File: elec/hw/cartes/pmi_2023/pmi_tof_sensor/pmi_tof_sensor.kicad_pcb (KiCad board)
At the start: 2 copper layers, 30 x 20 mm, 41 parts, among them J1 tof_sensor_female, U1 SN74LVC1T45DBV, U2 TMF8821, U3 VL53L1CXV0FY1, U4 VL53L5CXV0GC

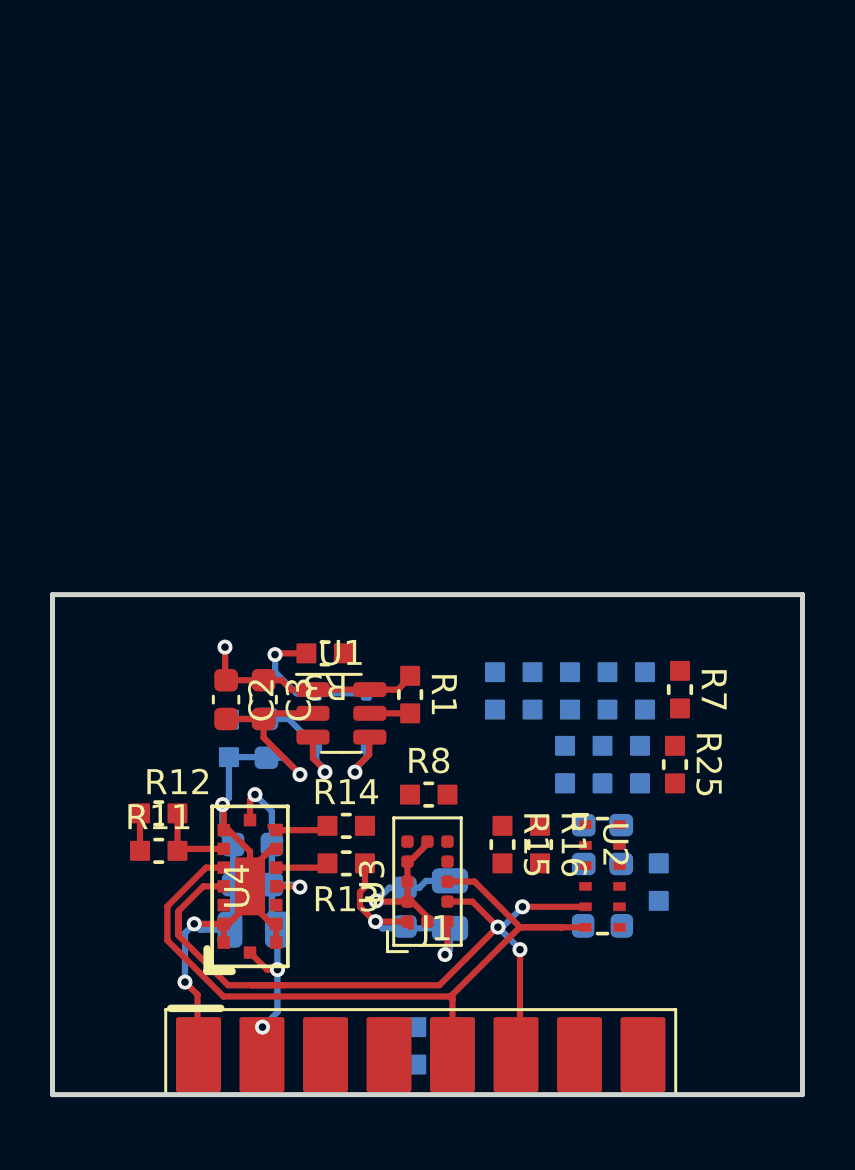
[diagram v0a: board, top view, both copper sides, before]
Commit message: pmi_tof_sensor : last commit before tmf8821 deletion
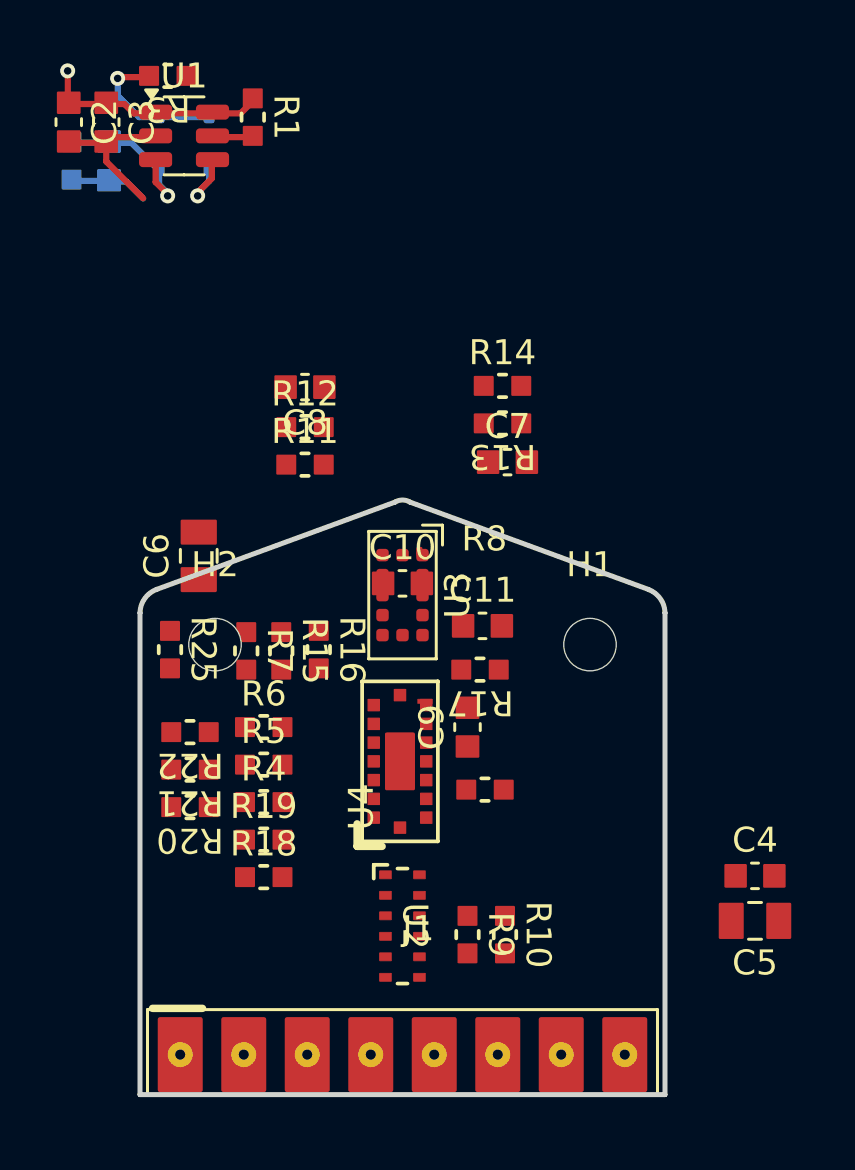
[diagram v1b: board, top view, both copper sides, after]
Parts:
- added H1: MountingHole, cocotter_others:MountingHole_2.1mm, F.Cu at (41.5, 162.0)
- added H2: MountingHole, cocotter_others:MountingHole_2.1mm, F.Cu at (26.5, 162.0)
- C10, C11, C4, C7, C8, C9, R18, R19, R20, R21, R22, R4, R5, R6: moved to F.Cu
- C5, C6: value 10µF 16V -> 10µF 25V; moved to F.Cu
- R1, R13, R14, R15, R16, R2, R25, R3, R7, R8: value 10k -> 10k 1%
- R10, R17, R9: value 10k -> 10k 1%; moved to F.Cu
- moved C1 23.9 mm to (22.3, 142.7)
- moved C2 23.9 mm to (20.6, 141.1)
- moved C3 23.9 mm to (22.1, 141.1)
- moved D1 23.9 mm to (24.3, 141.9)
- moved D2 23.9 mm to (26.3, 141.9)
- moved R1 23.9 mm to (28.0, 140.9)
- moved R2 23.9 mm to (20.8, 142.7)
- moved R3 23.9 mm to (24.6, 139.2)
- moved U1 23.9 mm to (25.3, 141.7)
- moved R25 20.7 mm to (24.7, 162.2)
- moved C7 19.7 mm to (38.2, 154.7), turned to 0 degrees
- moved R13 18.7 mm to (38.0, 153.2)
- moved R14 18.7 mm to (38.0, 151.7)
- moved C8 18.4 mm to (30.1, 151.7)
- moved R22 18.0 mm to (25.5, 165.5), turned to 180 degrees
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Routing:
- net GND: track 44.6 -> 9.56 mm, vias 5 -> 0
- net SCL_3v3: track 31.9 -> 0.00 mm, vias 3 -> 0
- net SDA_3v3: track 30.8 -> 0.00 mm
- net P3V3: track 36.0 -> 9.12 mm, vias 7 -> 1
- net /VL53L5_RSVD6_3v3: track 3.38 -> 0.00 mm
- net /VL53L5_irq_3v3: track 2.12 -> 0.00 mm
- net /VL53L5_I2C_RST_3v3: track 2.12 -> 0.00 mm
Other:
- board size 30 x 20 mm -> 21 x 23.8 mm

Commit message: pmi_tof_sensor : new form factor and enable sequencer
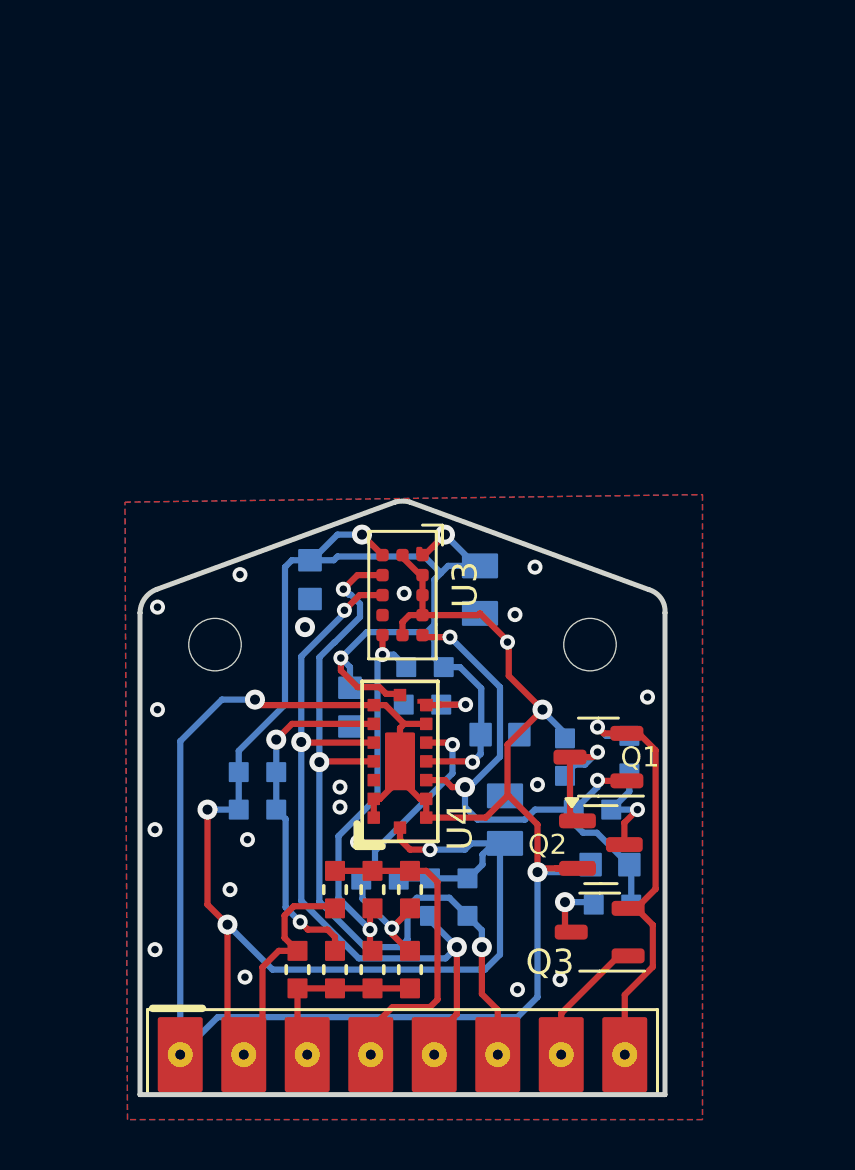
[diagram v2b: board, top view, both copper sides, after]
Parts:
- removed C1, C10, C11, C2, C3: 100nF 50V, cocotter_capacitors:C_0603_1608Metric
- removed D1, D2: 1SS367,H3F, Diode_SMD:D_SOD-323
- removed R1, R2, R3: 10k 1%, cocotter_resistor:r0603_reflow
- removed R19, R22: 0R, cocotter_resistor:r0603_reflow
- removed U1: SN74LVC1T45DBV, Package_TO_SOT_SMD:SOT-23-6
- removed U2: TMF8821, cocotter_ic:TMF882x
- added Q1: BSS84, cocotter_transistors:SOT-23-3, F.Cu at (41.8, 166.5)
- added Q2: 2N7002, Package_TO_SOT_SMD:SOT-23, F.Cu at (41.9, 170.0)
- added Q3: BSS84, cocotter_transistors:SOT-23-3, F.Cu at (41.9, 173.5)
- C4, C5, C6, C7, C8, C9, R10, R11, R12, R13, R14, R8, R9: moved to B.Cu
- R15, R17: value 10k 1% -> 100k; moved to B.Cu
- R16: value 10k 1% -> 3k3 1%; moved to B.Cu
- R18: value 0R -> 100k; moved to B.Cu
- moved C4 21.4 mm to (30.3, 159.4), turned to 90 degrees
- moved R13 18.9 mm to (33.1, 171.4)
- moved C5 17.2 mm to (37.1, 159.8), turned to -90 degrees
- moved C6 16.2 mm to (38.1, 169.0)
- moved R16 15.6 mm to (42.4, 172.4), turned to 0 degrees
- moved R18 15.4 mm to (43.1, 166.4), turned to 90 degrees
- moved R12 15.4 mm to (28.2, 168.6)
- moved R15 14.0 mm to (41.6, 168.6), turned to 180 degrees
- moved R14 13.1 mm to (34.8, 164.4), turned to 180 degrees
- moved C8 12.9 mm to (31.9, 164.5), turned to -90 degrees
- moved R7 12.9 mm to (29.8, 175.0)
- moved R11 12.4 mm to (28.2, 167.1)
- moved R25 11.6 mm to (31.3, 171.8), turned to 90 degrees
- moved C7 10.9 mm to (37.9, 165.6)
- moved R6 10.1 mm to (31.3, 175.0), turned to -90 degrees
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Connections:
- net SCL_3v3 renamed /SCL_3v3
- net SDA_3v3 renamed /SDA_3v3
- C4 pad 2: P3V3 -> +3.3V
- C5 pad 1: P3V3 -> +3.3V
- C6 pad 1: P3V3 -> +3.3V
- C7 pad 1: P3V3 -> +3.3V
- C8 pad 1: P3V3 -> +3.3V
- C9 pad 1: P3V3 -> /enable_tof_3v3
- J1 pad 2: P3V3 -> +3.3V
- J1 pad 7: /enable_tof_3v3 -> //enable_tof_3v3
- J1 pad 8: /reset_tof_com_3v3 -> //reset_tof_com_3v3
- R10 pad 1: P3V3 -> +3.3V
- R11 pad 1: P3V3 -> +3.3V
- R12 pad 1: P3V3 -> +3.3V
- R13 pad 1: P3V3 -> +3.3V
- R15 pad 1: P3V3 -> Net-(Q2-D)
- R15 pad 2: /TMF8821_IRQ_3v3 -> /enable_tof_3v3
- R16 pad 1: P3V3 -> Net-(Q3-D)
- R16 pad 2: /TMF8821_GPIO0_3v3 -> /enable_tof_3v3
- R17 pad 1: P3V3 -> Net-(Q1-D)
- R17 pad 2: /TMF8821_GPIO1_3v3 -> GND
- R18 pad 1: /TMF8821_GPIO0_3v3 -> Net-(Q2-D)
- R18 pad 2: enable_next_board_3v3 -> //reset_tof_com_3v3
- R25 pad 1: P3V3 -> +3.3V
- R7 pad 1: P3V3 -> +3.3V
- R8 pad 1: P3V3 -> +3.3V
- R9 pad 1: P3V3 -> +3.3V
- U3 pad 1: P3V3 -> +3.3V
- U3 pad 11: P3V3 -> +3.3V
- U4 pad A4: P3V3 -> +3.3V
- U4 pad B1: P3V3 -> +3.3V
- U4 pad B7: P3V3 -> +3.3V
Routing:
- net +3.3V: track 0.00 -> 93.4 mm, vias 0 -> 7
- net GND: track 9.56 -> 79.5 mm, vias 0 -> 23
- net /SCL_3v3: track 0.00 -> 32.1 mm, vias 0 -> 3
- net /SDA_3v3: track 0.00 -> 31.1 mm, vias 0 -> 3
- net /enable_tof_3v3: track 6.00 -> 24.1 mm, vias 1 -> 3
- net //reset_tof_com_3v3: track 0.00 -> 17.7 mm, vias 0 -> 1
- net /VL53L1_irq_3v3: track 0.00 -> 16.0 mm, vias 0 -> 2
- net /VL53L5_RSVD6_3v3: track 0.00 -> 14.2 mm, vias 0 -> 2
- net DETECT_IRQ_3v3: track 0.00 -> 13.2 mm
- net /VL53L5_irq_3v3: track 0.00 -> 12.7 mm, vias 0 -> 2
- net P3V3: track 9.12 -> 0.00 mm, vias 1 -> 0
- net enable_next_board_3v3: track 0.00 -> 7.31 mm
- net Net-(D1-K): track 6.56 -> 0.00 mm, vias 1 -> 0
- net Net-(Q1-D): track 0.00 -> 5.72 mm, vias 0 -> 1
- net //enable_tof_3v3: track 0.00 -> 5.28 mm
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- added copper zone on B.Cu, net GND
- added copper zone on F.Cu, net GND
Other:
- board size 21 x 23.8 mm -> 21 x 23.7 mm

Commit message: modified rc constant of enable circuit
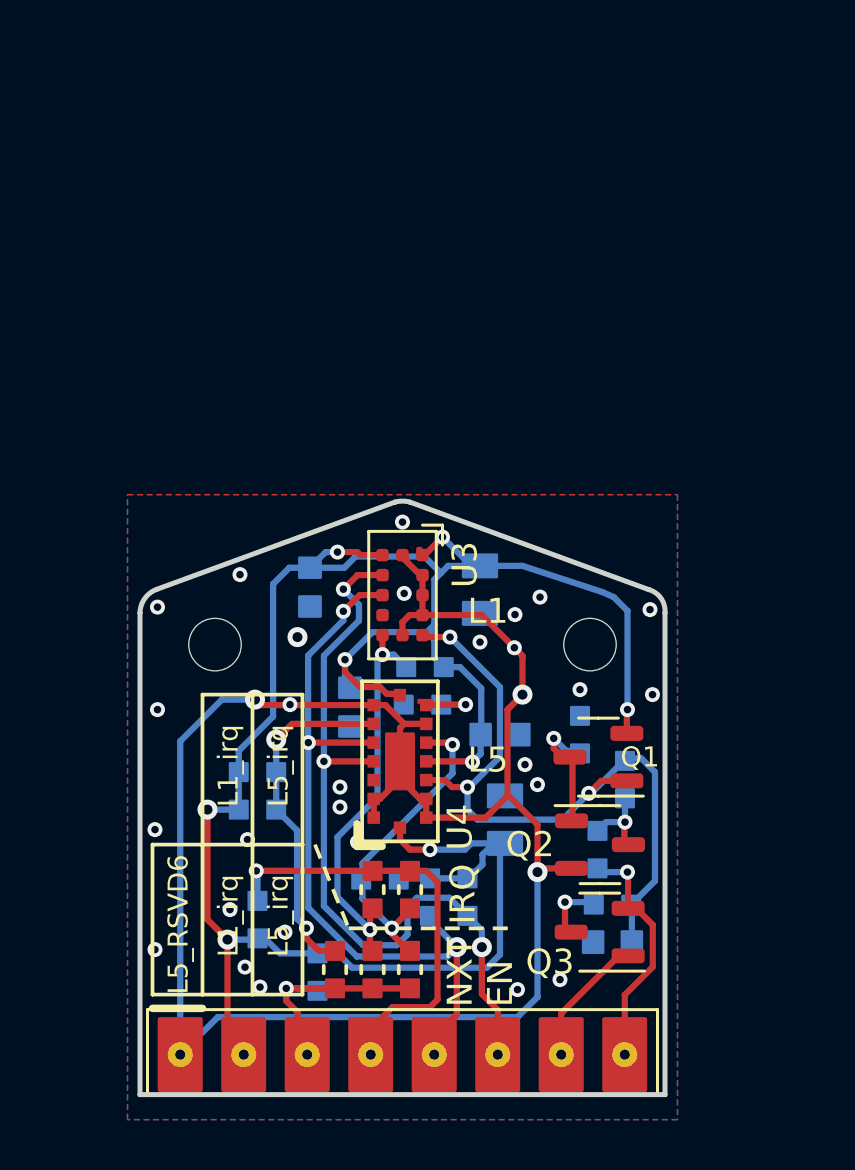
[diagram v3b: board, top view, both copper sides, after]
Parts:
- C9: value 100nF 50V -> 1nF 50V
- Q2: footprint Package_TO_SOT_SMD:SOT-23 -> cocotter_transistors:SOT-23-3
- R25, R7: moved to B.Cu
- moved R18 4.01 mm to (41.8, 170.2), turned to -90 degrees
- moved R25 3.32 mm to (28.2, 173.0)
- moved C9 3.10 mm to (42.4, 173.9)
- moved R15 1.77 mm to (42.9, 167.4), turned to 90 degrees
- moved R17 1.08 mm to (41.1, 165.6)
- moved R7 0.81 mm to (30.6, 175.1)
- moved C4 0.30 mm to (30.3, 159.7)
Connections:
- Q1 pad 2: //reset_tof_com_3v3 -> +3.3V
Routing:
- net //reset_tof_com_3v3: track 17.7 -> 9.64 mm
- net /enable_tof_3v3: track 24.1 -> 29.2 mm
- net GND: track 79.5 -> 75.0 mm, vias 23 -> 31
- net DETECT_IRQ_3v3: track 13.2 -> 17.5 mm, vias 0 -> 1
- net enable_next_board_3v3: track 7.31 -> 10.9 mm, vias 0 -> 1
- net +3.3V: track 93.4 -> 95.5 mm, vias 7 -> 8
- net Net-(Q2-D): track 4.42 -> 3.21 mm
- net /SDA_3v3: track 31.1 -> 30.2 mm
- net /SCL_3v3: track 32.1 -> 31.5 mm
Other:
- board text added: "IRQ"
- board text added: "L1"
- board text added: "L1_irq"
- board text added: "L5"
- board text added: "L5_RSVD6"
- board text added: "L5_irq"
- board text added: "NXT EN"
- board text added: "PMI_TOF_SENSOR"

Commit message: modified mounting hole, replaced transistors to place them in bottom layer
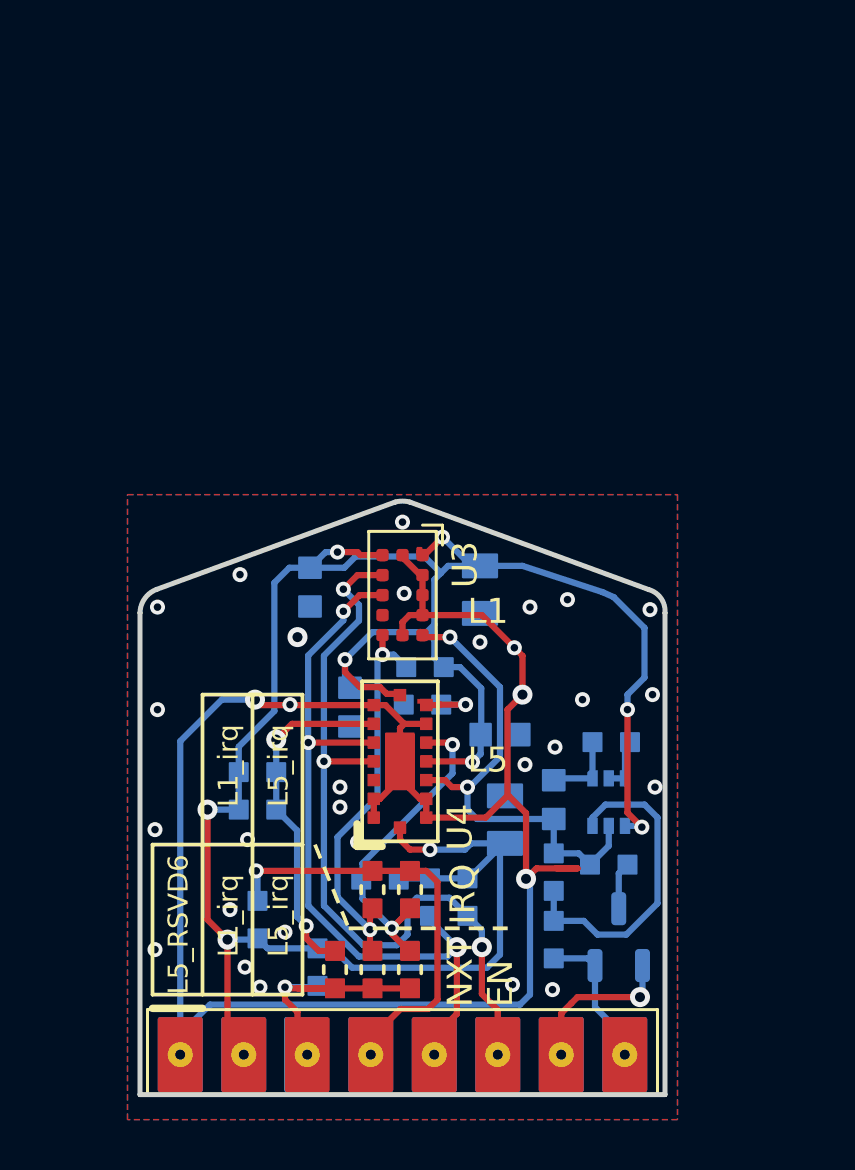
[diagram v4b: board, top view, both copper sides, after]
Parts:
- removed Q2: 2N7002, cocotter_transistors:SOT-23-3
- removed Q3: BSS84, cocotter_transistors:SOT-23-3
- added Q4: BSS8402DW-7-F, cocotter_transistors:SOT-363_SC-70-6, B.Cu at (42.2, 168.3)
- H1, H2: footprint cocotter_others:MountingHole_2.1mm -> cocotter_others:MountingHole_2.5mm-slot_1mm
- Q1: moved to B.Cu
- moved Q1 7.25 mm to (42.6, 173.7), turned to 90 degrees
- moved C9 6.17 mm to (40.0, 168.2), turned to 90 degrees
- moved R15 4.67 mm to (40.0, 171.1)
- moved R18 4.00 mm to (40.0, 173.8)
- moved R16 1.61 mm to (42.2, 170.8), turned to 180 degrees
- moved R17 1.29 mm to (42.4, 165.9), turned to 180 degrees
- moved R7 0.20 mm to (30.6, 174.9)
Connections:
- Q1 pad 1: /enable_tof_3v3 -> //enable_tof_3v3
- Q1 pad 2: +3.3V -> //reset_tof_com_3v3
- R16 pad 1: Net-(Q3-D) -> Net-(Q1-D)
- R17 pad 1: Net-(Q1-D) -> Net-(Q4A-GN)
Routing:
- net Net-(Q4A-DN): track 3.21 -> 12.9 mm, vias 1 -> 0
- net /enable_tof_3v3: track 29.2 -> 19.7 mm, vias 3 -> 2
- net +3.3V: track 95.5 -> 100.8 mm, vias 8 -> 9
- net //reset_tof_com_3v3: track 9.64 -> 5.82 mm, vias 1 -> 0
- net GND: track 75.0 -> 78.6 mm, vias 31 -> 32
- net Net-(Q1-D): track 5.37 -> 1.91 mm, vias 1 -> 0
- net Net-(Q3-D): track 2.49 -> 0.00 mm, vias 1 -> 0
- net Net-(Q4A-GN): track 0.00 -> 2.18 mm
- net //enable_tof_3v3: track 5.28 -> 6.37 mm, vias 0 -> 1

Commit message: bom updated and component selection optimized to decrease bom cost
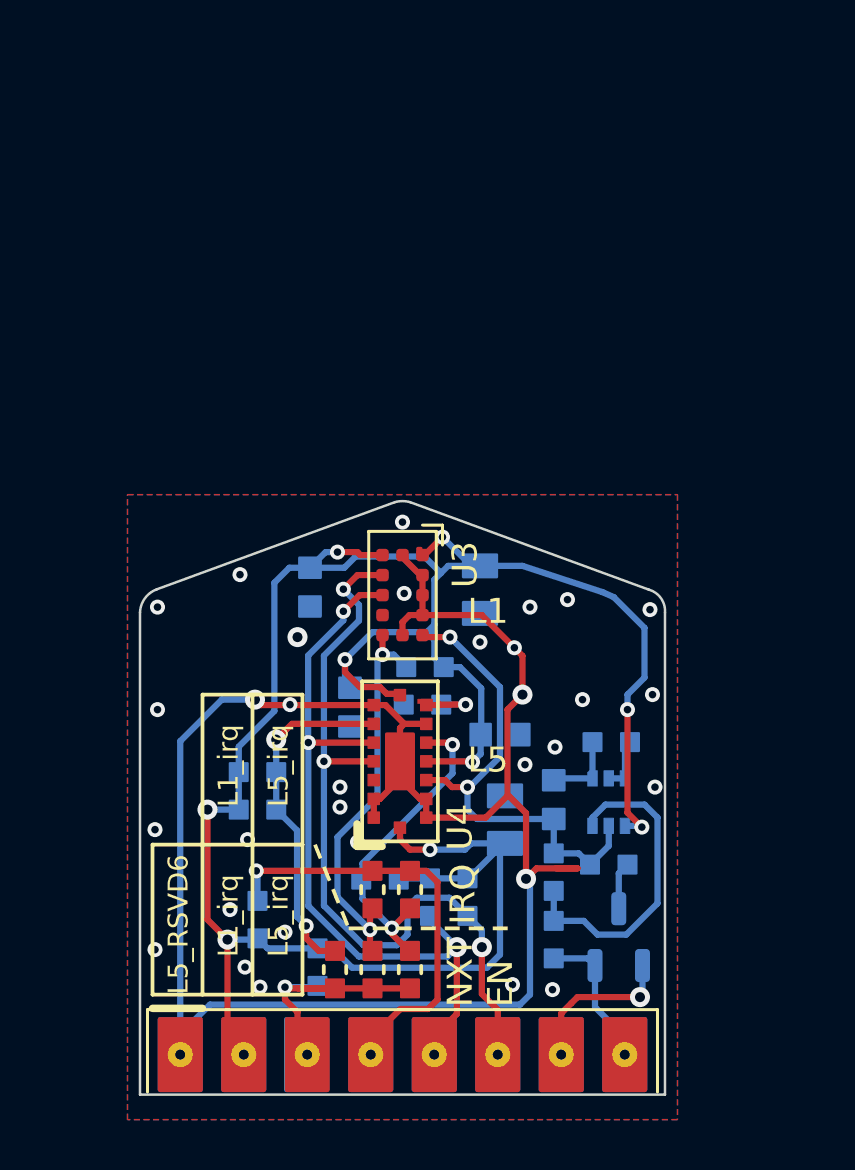
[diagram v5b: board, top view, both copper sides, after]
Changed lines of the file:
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@@
 		(sheetname "Racine")
 		(sheetfile "pmi_tof_sensor.kicad_sch")
-		(attr smd)
+		(attr smd dnp)
 		(fp_line
 			(start -1.07 -1.815)
@@
 		(end 23.5 160.73)
 		(stroke
-			(width 0.2)
+			(width 0.1)
 			(type default)
 		)
@@
 		(end 44.5 180)
 		(stroke
-			(width 0.2)
+			(width 0.1)
 			(type default)
 		)
@@
 		(end 44.5 160.73)
 		(stroke
-			(width 0.2)
+			(width 0.1)
 			(type default)
 		)
@@
 		(end 44.5 180)
 		(stroke
-			(width 0.2)
+			(width 0.1)
 			(type default)
 		)
@@
 		(end 34.3 156.3)
 		(stroke
-			(width 0.2)
+			(width 0.1)
 			(type default)
 		)
@@
 		(end 24.166637 159.790798)
 		(stroke
-			(width 0.2)
+			(width 0.1)
 			(type default)
 		)
@@
 		(end 33.7 156.3)
 		(stroke
-			(width 0.2)
+			(width 0.1)
 			(type default)
 		)
@@
 		(end 43.85 159.8)
 		(stroke
-			(width 0.2)
+			(width 0.1)
 			(type default)
 		)
